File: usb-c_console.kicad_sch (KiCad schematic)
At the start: 28 parts, among them J3 USB-C_Kycon_KUSBX-SL2-CS1N24-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, U6 FT230X_QFN, U7 NTS0102_TSSOP

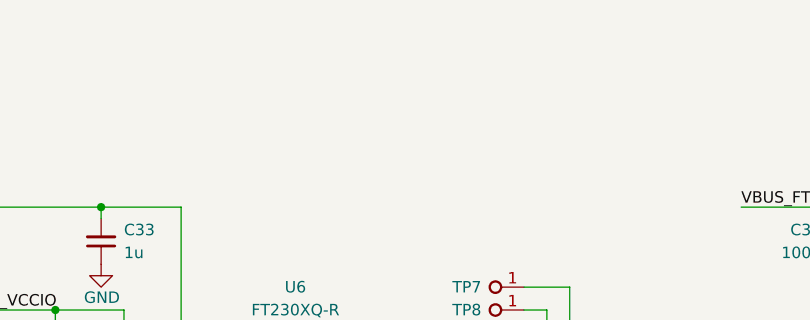
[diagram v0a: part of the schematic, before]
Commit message: [#70030] Unify functional block names
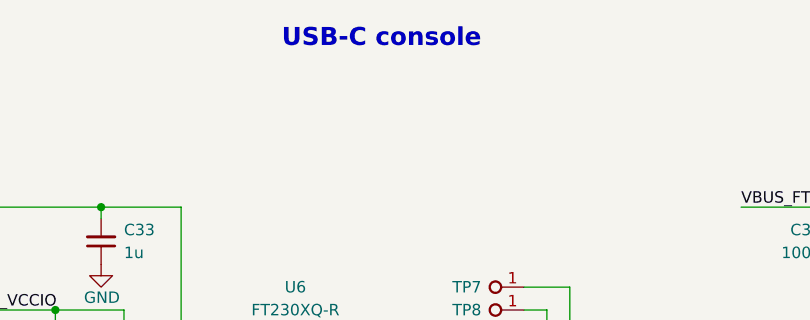
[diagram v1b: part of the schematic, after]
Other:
- note added: "USB-C console"
- company: Antmicro Ltd. -> Antmicro Ltd
- title: Com Express 7 baseboard -> COM Express 7 Baseboard
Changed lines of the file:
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@@
 	(paper "A3")
 	(title_block
-		(title "Com Express 7 baseboard")
-		(date "2024-03-28")
+		(title "COM Express 7 Baseboard")
+		(date "2024-12-13")
 		(rev "1.1.0")
-		(company "Antmicro Ltd.")
+		(company "Antmicro Ltd")
+		(comment 1 "www.antmicro.com")
 	)
 	(bus_alias "UART"
@@
 		)
 	)
+	(text "USB-C console"
+		(exclude_from_sim no)
+		(at 200.406 94.234 0)
+		(effects
+			(font
+				(size 2 2)
+				(thickness 0.4)
+				(bold yes)
+			)
+			(justify left bottom)
+		)
+	)
